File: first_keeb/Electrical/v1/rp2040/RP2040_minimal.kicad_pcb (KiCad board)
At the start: 4 copper layers, 67.1 x 66.8 mm, 71 parts, among them J1 Conn_01x04_Socket, P1 USB-TYPE-C-016, Q1 BSS138, SW1 TS-1187A-B-A-B, SW2 TS-1187A-B-A-B, SW3 BUTT1, SW4 BUTT3, SW5 BUTT2, U1 ME6208A44M3G, U2 ME6212C25M5G, U3 PRTR5V0U2X, U4 SLSS49E, U5 SLSS49E, U6 SLSS49E, U7 STM32F401RCTx, Y1 8MHz

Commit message: finishes rp2040 v1
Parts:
- removed the C14 at (83.9, 87.9)
- removed the C20 at (94.6, 94.3)
- removed FB1: GZ2012D601TF, Capacitor_SMD:C_0805_2012Metric
- removed the U7 at (91.4, 85.7)
- added C10: 1u, Capacitor_SMD:C_0402_1005Metric, F.Cu at (95.4, 89.8)
- added C18: 10u, Capacitor_SMD:C_1206_3216Metric, F.Cu at (108.0, 84.7)
- added C19: 10u, Capacitor_SMD:C_1206_3216Metric, F.Cu at (101.5, 84.7)
- added C7: 100n, Capacitor_SMD:C_0402_1005Metric, F.Cu at (91.8, 82.3)
- added C8: 100n, Capacitor_SMD:C_0402_1005Metric, F.Cu at (93.5, 92.0)
- added C9: 1u, Capacitor_SMD:C_0402_1005Metric, F.Cu at (97.5, 90.2)
- added R3: 27R, Capacitor_SMD:C_0402_1005Metric, F.Cu at (97.5, 87.8)
- added R6: 1k, Capacitor_SMD:C_0402_1005Metric, F.Cu at (80.7, 77.7)
- added U3: RP2040, MCU_RaspberryPi_and_Boards:RP2040-QFN-56, F.Cu at (90.3, 87.0)
- added U5: W25Q16JVSS, Package_SO:SOIC-8_5.23x5.23mm_P1.27mm, F.Cu at (87.2, 78.3)
- added U6: ME6212C33M5G, Package_TO_SOT_SMD:SOT-23-5, F.Cu at (104.7, 85.3)
- C1: value 4u7 -> 100n; footprint Capacitor_SMD:C_0603_1608Metric -> Capacitor_SMD:C_0402_1005Metric
- C11: moved to F.Cu
- C13: value 1u -> 100n
- Q1: moved to B.Cu
- R4: value 10k -> 27R; footprint Resistor_SMD:R_0402_1005Metric -> Capacitor_SMD:C_0402_1005Metric; moved to F.Cu
- R5: footprint Resistor_SMD:R_0402_1005Metric -> Capacitor_SMD:C_0402_1005Metric
- R8: renamed from R6; moved to B.Cu
- R9: renamed from R7; moved to B.Cu
- moved R5 21.4 mm to (81.7, 76.5), turned to -90 degrees
- moved R8 18.9 mm to (93.1, 81.4)
- moved C13 15.3 mm to (92.3, 75.9)
- moved R4 13.7 mm to (97.5, 88.8)
- moved Q1 13.6 mm to (95.7, 81.1), turned to 0 degrees
- moved C3 13.6 mm to (88.7, 91.9), turned to 180 degrees
- moved C4 13.0 mm to (83.9, 87.3), turned to 180 degrees
- moved C1 12.7 mm to (96.9, 85.4), turned to 90 degrees
- moved C12 12.5 mm to (95.4, 91.8), turned to 0 degrees
- moved C5 10.8 mm to (96.9, 86.9), turned to 0 degrees
- moved C6 9.80 mm to (87.9, 82.3), turned to 180 degrees
- moved SW2 9.11 mm to (82.7, 88.5)
- moved C11 8.81 mm to (95.4, 90.8), turned to 0 degrees
- moved R9 8.72 mm to (98.2, 80.6)
- moved C2 6.25 mm to (83.9, 88.3)
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- renumbered C7 to C14, C8 to C15, C9 to C16, C10 to C17, C18 to C20, C19 to C21, C15 to C22, C16 to C23, C17 to C24, C21 to C25, C22 to C26, C23 to C27, C24 to C28, C25 to C29, C26 to C30, C27 to C31, C28 to C32, C29 to C33, C30 to C34, R3 to R7, U3 to U1, U1 to U2, U2 to U4, U6 to U7, U4 to U8, U5 to U9
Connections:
- C1 pad 1: VDD -> +1V1
- C11 pad 1: NRST -> ADC_AVDD
- C12 pad 1: VDD -> ADC_AVDD
- C13 pad 1: VDDA -> +3V3
- C17 pad 1: VDD -> ADC_AVDD
- C2 pad 1: VDD -> +1V1
- C3 pad 1: VDD -> +3V3
- C4 pad 1: VDD -> +3V3
- C5 pad 1: VDD -> +3V3
- C6 pad 1: VDD -> +3V3
- J1 pad 1: VDD -> +3V3
- J1 pad 2: SWDIO -> SWCLK
- J1 pad 3: SWCLK -> SWDIO
- Q1 pad 1: VDD -> +3V3
- R4 pad 1: BOOT0 -> USB_D-
- R4 pad 2: GND -> Net-(U3-USB_DM)
- R5 pad 1: GND -> +3V3
- R5 pad 2: BOOT1 -> /QSPI_SS
- R8 pad 2: VDD -> +3V3
- SW1 pad 1: BOOT0 -> GND
- SW1 pad 2: VDD -> Net-(R6-Pad1)
- SW2 pad 1: NRST -> GND
- SW2 pad 2: GND -> Net-(U3-RUN)
- U4 pad 5: VDD -> ADC_AVDD
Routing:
- net +3V3: track 0.00 -> 79.9 mm, vias 0 -> 6
- net VDD: track 76.9 -> 0.00 mm, vias 2 -> 0
- net SWCLK: track 12.8 -> 42.7 mm
- net SWDIO: track 21.5 -> 46.8 mm, vias 2 -> 0
- net /QSPI_SS: track 0.00 -> 21.3 mm
- net /QSPI_SD1: track 0.00 -> 19.0 mm
- net +1V1: track 0.00 -> 18.0 mm, vias 0 -> 4
- net /QSPI_SD2: track 0.00 -> 16.6 mm
- net ADC_AVDD: track 0.00 -> 14.8 mm
- net /QSPI_SD3: track 0.00 -> 13.4 mm
- net Net-(R6-Pad1): track 0.00 -> 13.4 mm, vias 0 -> 1
- net /QSPI_SCLK: track 0.00 -> 11.7 mm
- net BOOT1: track 10.6 -> 0.00 mm, vias 2 -> 0
- net NRST: track 10.3 -> 0.00 mm, vias 1 -> 0
- net /QSPI_SD0: track 0.00 -> 10.0 mm
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- added copper zone on F.Cu, net +1V1
- added copper zone on F.Cu, net +3V3

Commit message: adds 10n and 100n capactiros near rp2040 adc_avdd
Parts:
- C11: value 100n -> 10n
- C12: value 1u -> 100n
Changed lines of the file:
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@@
         (effects (font (size 1 1) (thickness 0.15)))
     )
-    (fp_text value "1u" (at 0 1.16) (layer "F.Fab")
+    (fp_text value "100n" (at 0 1.16) (layer "F.Fab")
         (effects (font (size 1 1) (thickness 0.15)))
     )
@@
         (effects (font (size 1 1) (thickness 0.15)))
     )
-    (fp_text value "100n" (at 0 1.16) (layer "F.Fab")
-        (effects (font (size 1 1) (thickness 0.15)))
-    )
+    (fp_text value "10n" (at 0 1.16) (layer "F.Fab")
+        (effects (font (size 1 1) (thickness 0.15)))
+    )

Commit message: puts 10n and 1u caps to decouple adv_avdd on rp2040 to match the stm32 adc vref
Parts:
- C12: value 100n -> 1u
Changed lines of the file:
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@@
         (effects (font (size 1 1) (thickness 0.15)))
     )
-    (fp_text value "100n" (at 0 1.16) (layer "F.Fab")
+    (fp_text value "1u" (at 0 1.16) (layer "F.Fab")
         (effects (font (size 1 1) (thickness 0.15)))
     )

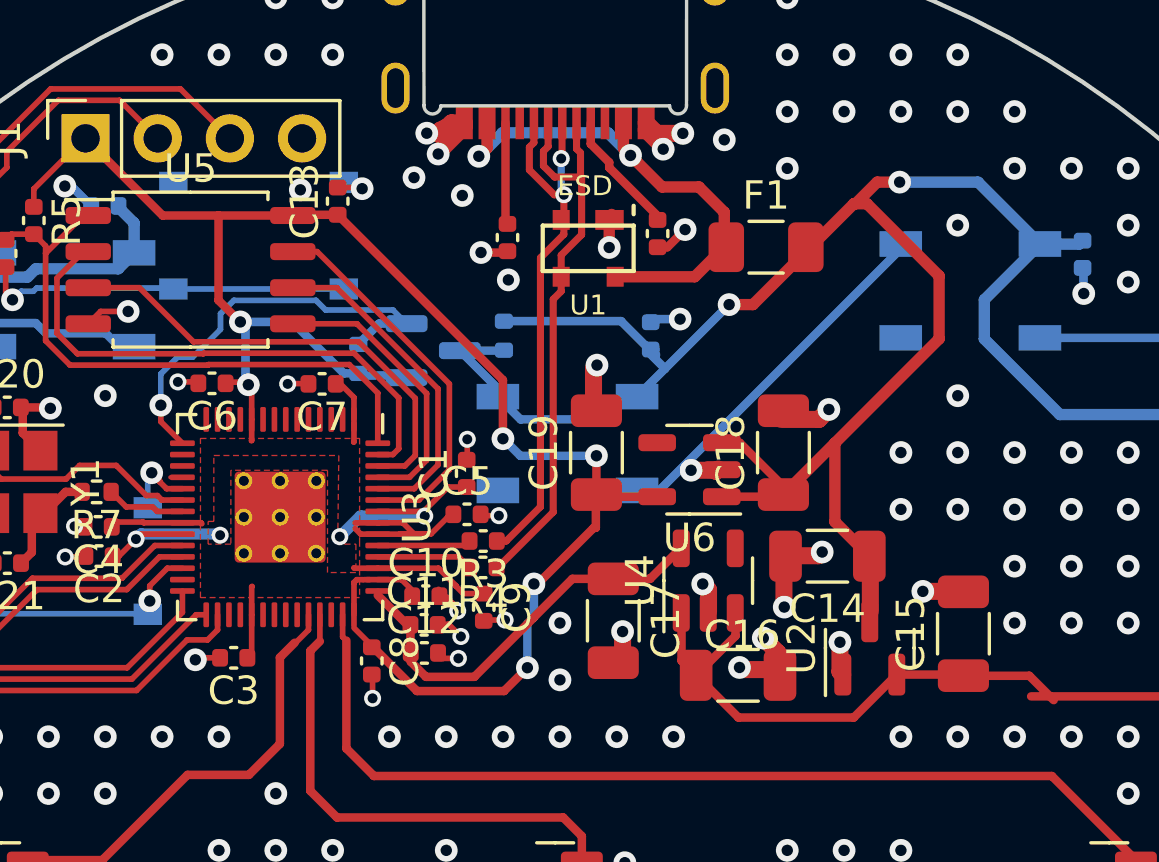
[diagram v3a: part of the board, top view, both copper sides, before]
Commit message: generates assembly files
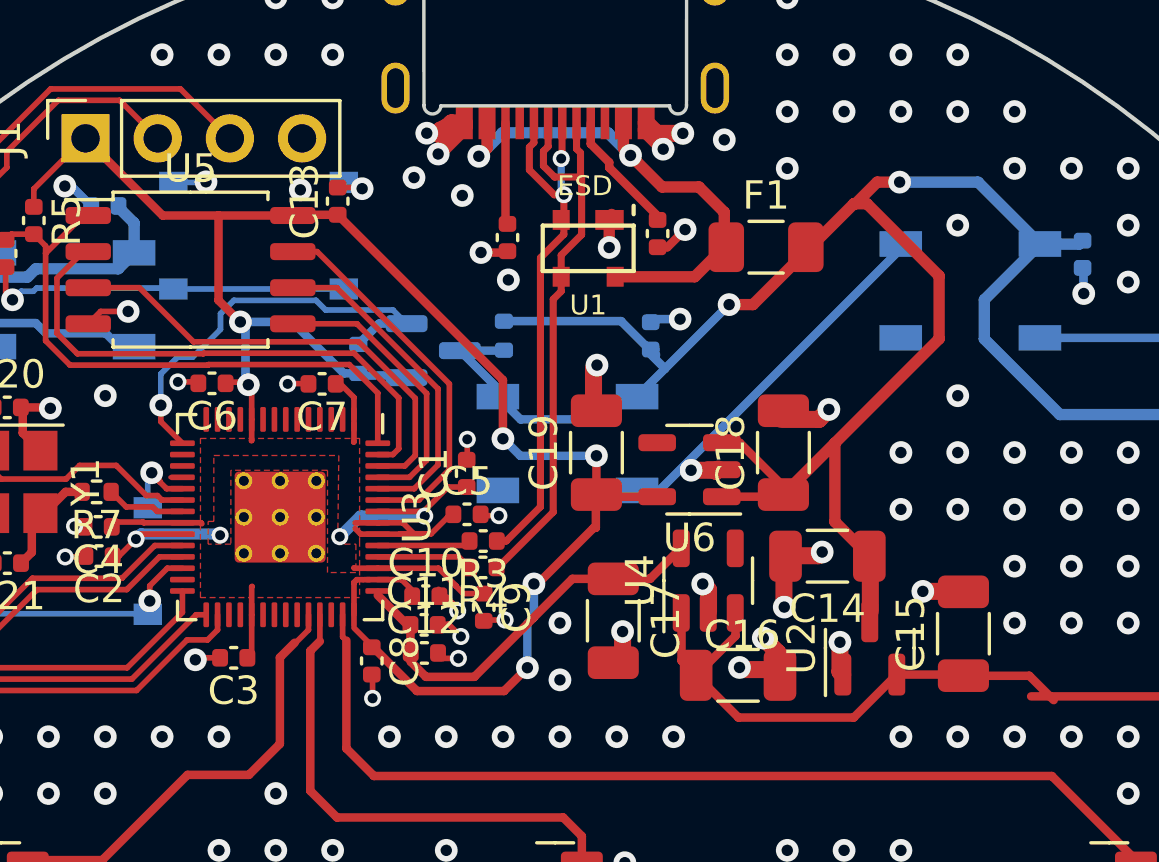
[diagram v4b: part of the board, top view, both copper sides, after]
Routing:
- net GND: track 80.1 -> 81.4 mm, vias 316 -> 317
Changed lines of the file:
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@@
     (fp_line (start 1.6 0.8) (end -1.6 0.8)
       (stroke (width 0.1) (type solid)) (layer "F.Fab"))
-    (pad "1" smd roundrect (at -1.475 0 90) (size 1.15 1.8) (layers "F.Cu" "F.Paste" "F.Mask") (roundrect_rratio 0.217391)
+    (pad "1" smd roundrect (at -1.475 0 90) (size 1.15 1.8) (layers "F.Cu" "F.Paste" "F.Mask") (roundrect_rratio 0.2173913043)
       (net 5 "+5V") (pintype "passive"))
-    (pad "2" smd roundrect (at 1.475 0 90) (size 1.15 1.8) (layers "F.Cu" "F.Paste" "F.Mask") (roundrect_rratio 0.217391)
+    (pad "2" smd roundrect (at 1.475 0 90) (size 1.15 1.8) (layers "F.Cu" "F.Paste" "F.Mask") (roundrect_rratio 0.2173913043)
       (net 1 "GND") (pintype "passive"))
     (model "${KICAD6_3DMODEL_DIR}/Capacitor_SMD.3dshapes/C_1206_3216Metric.wrl"
@@
     (fp_line (start 3.5 3.5) (end -3.5 3.5)
       (stroke (width 0.1) (type solid)) (layer "F.Fab"))
-    (pad "" smd roundrect (at -0.6375 -0.6375 270) (size 1.084435 1.084435) (layers "F.Paste") (roundrect_rratio 0.230535))
-    (pad "" smd roundrect (at -0.6375 0.6375 270) (size 1.084435 1.084435) (layers "F.Paste") (roundrect_rratio 0.230535))
-    (pad "" smd roundrect (at 0.6375 -0.6375 270) (size 1.084435 1.084435) (layers "F.Paste") (roundrect_rratio 0.230535))
-    (pad "" smd roundrect (at 0.6375 0.6375 270) (size 1.084435 1.084435) (layers "F.Paste") (roundrect_rratio 0.230535))
+    (pad "" smd roundrect (at -0.6375 -0.6375 270) (size 1.084435 1.084435) (layers "F.Paste") (roundrect_rratio 0.2305347946))
+    (pad "" smd roundrect (at -0.6375 0.6375 270) (size 1.084435 1.084435) (layers "F.Paste") (roundrect_rratio 0.2305347946))
+    (pad "" smd roundrect (at 0.6375 -0.6375 270) (size 1.084435 1.084435) (layers "F.Paste") (roundrect_rratio 0.2305347946))
+    (pad "" smd roundrect (at 0.6375 0.6375 270) (size 1.084435 1.084435) (layers "F.Paste") (roundrect_rratio 0.2305347946))
     (pad "1" smd roundrect (at -3.4375 -2.6 270) (size 0.875 0.2) (layers "F.Cu" "F.Paste" "F.Mask") (roundrect_rratio 0.25)
       (net 36 "+3V3") (pinfunction "IOVDD") (pintype "power_in"))
@@
     (fp_line (start 1.6 0.8) (end -1.6 0.8)
       (stroke (width 0.1) (type solid)) (layer "F.Fab"))
-    (pad "1" smd roundrect (at -1.475 0 90) (size 1.15 1.8) (layers "F.Cu" "F.Paste" "F.Mask") (roundrect_rratio 0.217391)
+    (pad "1" smd roundrect (at -1.475 0 90) (size 1.15 1.8) (layers "F.Cu" "F.Paste" "F.Mask") (roundrect_rratio 0.2173913043)
       (net 32 "+4V4") (pintype "passive"))
-    (pad "2" smd roundrect (at 1.475 0 90) (size 1.15 1.8) (layers "F.Cu" "F.Paste" "F.Mask") (roundrect_rratio 0.217391)
+    (pad "2" smd roundrect (at 1.475 0 90) (size 1.15 1.8) (layers "F.Cu" "F.Paste" "F.Mask") (roundrect_rratio 0.2173913043)
       (net 1 "GND") (pintype "passive"))
     (model "${KICAD6_3DMODEL_DIR}/Capacitor_SMD.3dshapes/C_1206_3216Metric.wrl"
@@
     (fp_line (start 1.6 0.8) (end -1.6 0.8)
       (stroke (width 0.1) (type solid)) (layer "F.Fab"))
-    (pad "1" smd roundrect (at -1.475 0 90) (size 1.15 1.8) (layers "F.Cu" "F.Paste" "F.Mask") (roundrect_rratio 0.217391)
+    (pad "1" smd roundrect (at -1.475 0 90) (size 1.15 1.8) (layers "F.Cu" "F.Paste" "F.Mask") (roundrect_rratio 0.2173913043)
       (net 36 "+3V3") (pintype "passive"))
-    (pad "2" smd roundrect (at 1.475 0 90) (size 1.15 1.8) (layers "F.Cu" "F.Paste" "F.Mask") (roundrect_rratio 0.217391)
+    (pad "2" smd roundrect (at 1.475 0 90) (size 1.15 1.8) (layers "F.Cu" "F.Paste" "F.Mask") (roundrect_rratio 0.2173913043)
       (net 1 "GND") (pintype "passive"))
     (model "${KICAD6_3DMODEL_DIR}/Capacitor_SMD.3dshapes/C_1206_3216Metric.wrl"
@@
         (effects (font (size 1 1) (thickness 0.15)) (justify mirror))
     )
+    (fp_text user "BOOTSEL" (at 0.13 -2.845 unlocked) (layer "B.SilkS")
+        (effects (font (size 1 1) (thickness 0.15)) (justify mirror))
+    )
     (fp_text user "${REFERENCE}" (at 0 -2.5 unlocked) (layer "B.Fab")
         (effects (font (size 1 1) (thickness 0.15)) (justify mirror))
@@
         (effects (font (size 1 1) (thickness 0.15)) (justify mirror))
     )
+    (fp_text user "RUN" (at -0.17 -2.975 unlocked) (layer "B.SilkS")
+        (effects (font (size 1 1) (thickness 0.15)) (justify mirror))
+    )
     (fp_text user "${REFERENCE}" (at 0 -2.5 unlocked) (layer "B.Fab")
         (effects (font (size 1 1) (thickness 0.15)) (justify mirror))
@@
   (via (at 126.166 106.706) (size 0.8) (drill 0.4) (layers "F.Cu" "B.Cu") (free) (net 1))
   (via (at 82.166 94.706) (size 0.8) (drill 0.4) (layers "F.Cu" "B.Cu") (free) (net 1))
+  (via (at 87.71 75.18) (size 0.8) (drill 0.4) (layers "F.Cu" "B.Cu") (net 1))
   (via (at 114.166 114.706) (size 0.8) (drill 0.4) (layers "F.Cu" "B.Cu") (free) (net 1))
   (via (at 74.166 112.706) (size 0.8) (drill 0.4) (layers "F.Cu" "B.Cu") (free) (net 1))
@@
   (segment (start 126.09 116.6) (end 126.065 116.625) (width 0.3) (layer "B.Cu") (net 1))
   (segment (start 79.45 86.65) (end 78.83 86.03) (width 0.2) (layer "B.Cu") (net 1))
+  (segment (start 87.71 75.12) (end 87.64 75.19) (width 0.2) (layer "B.Cu") (net 1))
   (segment (start 82 115.43) (end 83.07 115.43) (width 0.3) (layer "B.Cu") (net 1))
   (segment (start 83.67 76.03) (end 82.97 75.33) (width 0.3) (layer "B.Cu") (net 1))
@@
   (segment (start 123.53 107.14) (end 123.535 107.145) (width 0.3) (layer "B.Cu") (net 1))
   (segment (start 79.181907 82.3) (end 79.161907 82.28) (width 0.3) (layer "B.Cu") (net 1))
+  (segment (start 87.63 75.2) (end 87.65 75.18) (width 0.2) (layer "B.Cu") (net 1))
   (segment (start 88.09 120.66) (end 85.1475 120.66) (width 0.3) (layer "B.Cu") (net 1))
   (segment (start 100 120.6) (end 99.92 120.68) (width 0.3) (layer "B.Cu") (net 1))
@@
   (segment (start 112.23 120.62) (end 114.605 120.62) (width 0.3) (layer "B.Cu") (net 1))
   (segment (start 118.59 79.1) (end 118.59 79.15) (width 0.3) (layer "B.Cu") (net 1))
+  (segment (start 87.71 75.18) (end 87.71 75.12) (width 0.2) (layer "B.Cu") (net 1))
   (segment (start 79.66 86.65) (end 79.45 86.65) (width 0.2) (layer "B.Cu") (net 1))
   (segment (start 109.375 120.6) (end 109.395 120.62) (width 0.3) (layer "B.Cu") (net 1))
@@
   (segment (start 123.535 107.195) (end 123.51 107.22) (width 0.3) (layer "B.Cu") (net 1))
   (segment (start 84.545 107.085) (end 84.545 107.135) (width 0.3) (layer "B.Cu") (net 1))
+  (segment (start 87.65 75.18) (end 87.71 75.18) (width 0.2) (layer "B.Cu") (net 1))
   (segment (start 93.13 123.17) (end 93.08 123.17) (width 0.3) (layer "B.Cu") (net 1))
   (segment (start 102.625 120.6) (end 102.545 120.68) (width 0.3) (layer "B.Cu") (net 1))
   (segment (start 126.09 116.55) (end 126.09 116.6) (width 0.3) (layer "B.Cu") (net 1))
+  (segment (start 86.56 75.2) (end 87.63 75.2) (width 0.2) (layer "B.Cu") (net 1))
   (segment (start 84.545 106.185) (end 84.545 107.075) (width 0.3) (layer "B.Cu") (net 1))
   (segment (start 99.92 120.68) (end 97.455 120.68) (width 0.3) (layer "B.Cu") (net 1))

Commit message: make bottom hole
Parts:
- H3: value MountingHole_3.2mm_M3_DIN965 -> MountingHole_4.3mm_M4_DIN965; footprint MountingHole:MountingHole_3.2mm_M3_DIN965 -> MountingHole:MountingHole_4.3mm_M4_DIN965
- moved H1 1.00 mm to (123.5, 88.0)
- moved H2 1.00 mm to (76.5, 88.0)
- moved SW2 0.77 mm to (83.4, 88.4)
- moved C21 0.64 mm to (81.2, 88.2)
- moved C20 0.52 mm to (81.2, 82.9)
- moved Y1 0.52 mm to (81.5, 85.5)
- moved R7 0.38 mm to (84.2, 86.2)
- moved C2 0.36 mm to (83.8, 88.7)
- moved C4 0.27 mm to (84.1, 87.2)
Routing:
- net GND: track 81.4 -> 84.7 mm, vias 317 -> 312
- net OSC_IN: track 9.76 -> 8.68 mm
- net +3V3: track 79.9 -> 79.3 mm

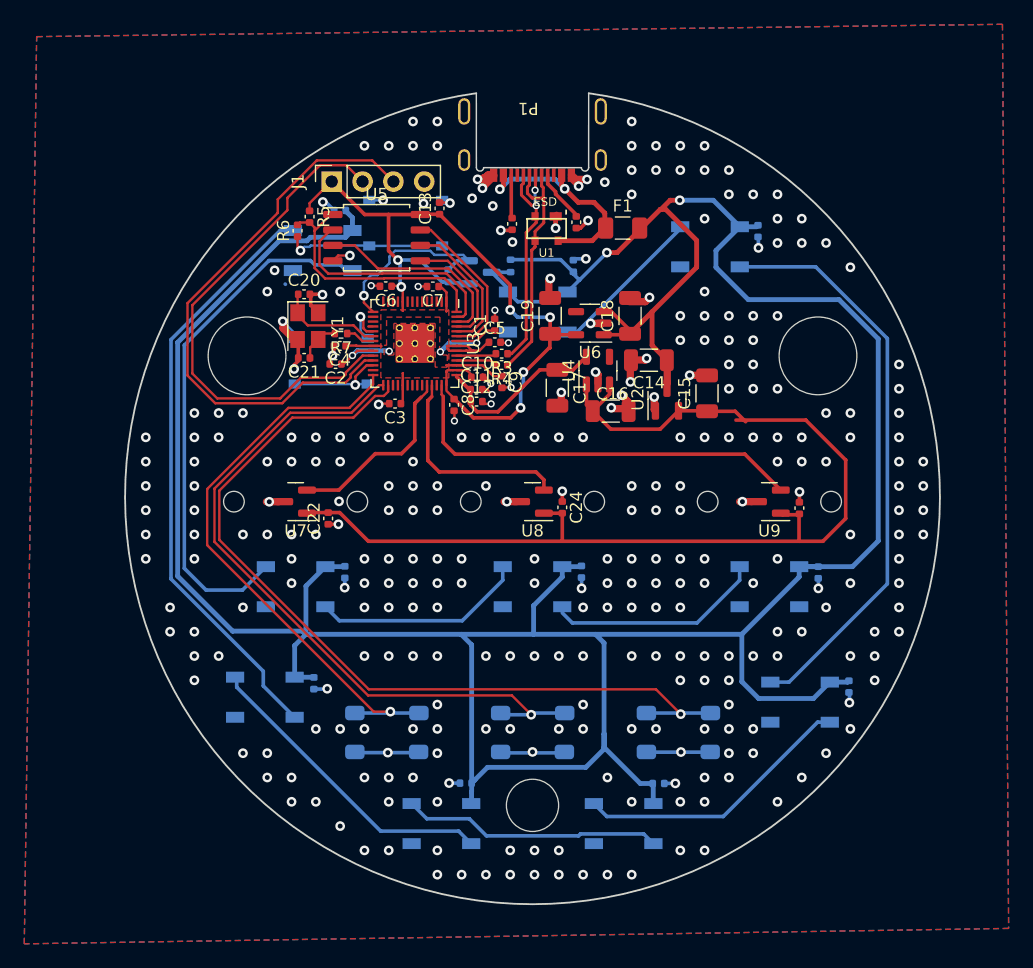
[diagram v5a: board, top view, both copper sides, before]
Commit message: moves plates together
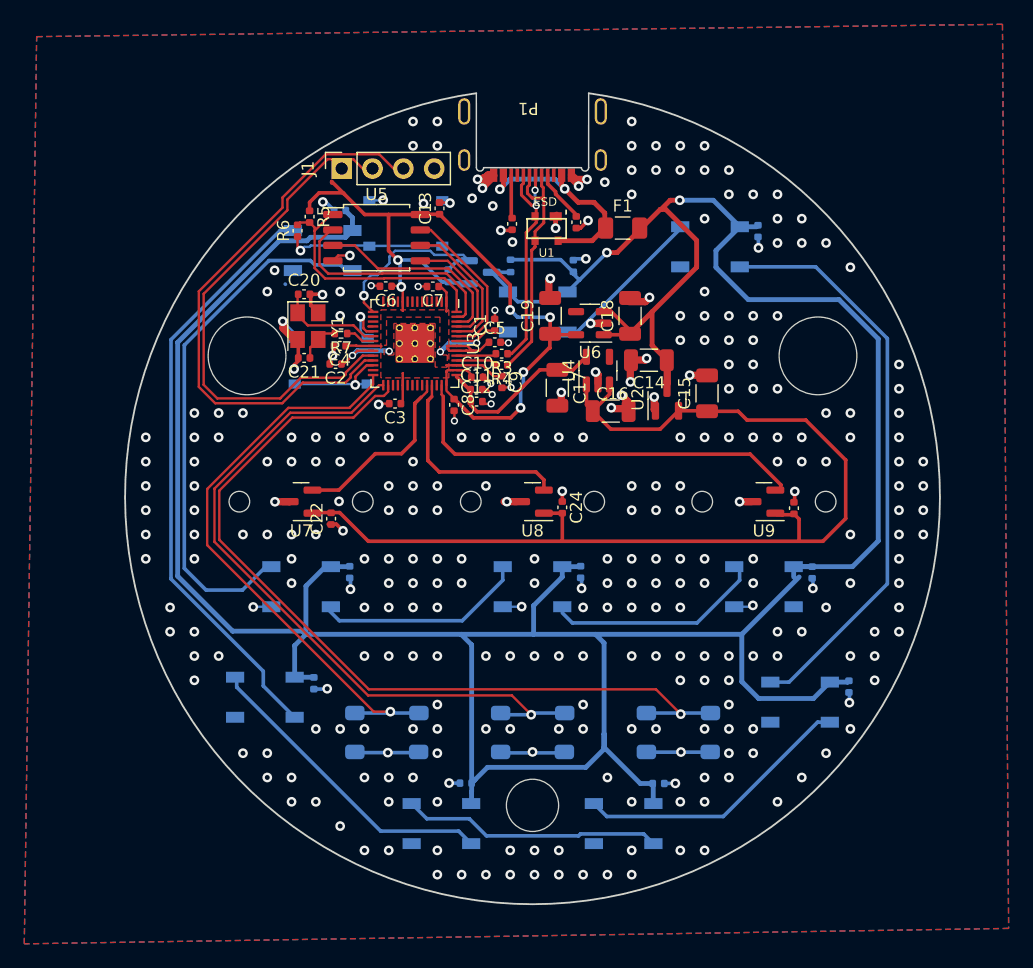
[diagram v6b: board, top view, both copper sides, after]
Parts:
- C20, C21: value 12p -> 27p
- Y1: value 8MHz -> 12MHz
- moved J1 1.35 mm to (84.3, 72.6)
- moved C27 0.50 mm to (123.0, 105.8)
- moved C23 0.45 mm to (121.5, 100.5)
- moved D1 0.45 mm to (81.0, 107.0)
- moved D3 0.45 mm to (119.0, 107.0)
- moved REF** 0.45 mm to (119.0, 100.0)
- moved REF** 0.45 mm to (81.0, 100.0)
- moved U7 0.45 mm to (81.0, 100.0)
- moved U9 0.45 mm to (119.0, 100.0)
- moved C25 0.40 mm to (85.0, 105.8)
- moved C22 0.24 mm to (83.4, 101.4)
- moved C26 0.07 mm to (104.0, 105.8)
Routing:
- net GND: track 84.7 -> 90.5 mm, vias 312 -> 313
- net +3V3: track 79.3 -> 80.7 mm
- net +4V4: track 88.3 -> 87.6 mm
